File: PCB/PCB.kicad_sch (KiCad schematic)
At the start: 32 parts, among them J1 Conn_01x10_Socket, J10 DMX-OUT, J2 Conn_01x06, J3 Screw_Terminal_01x02, J4 TEST_1P, J5 DMX-IN, J6 TEST_1P, Q1 BC847W, Q2 BC847W, Q3 BC847W, SW2 SW_Coded_SH-7010, U1 SP3485CN, U3 ESP32-WROOM

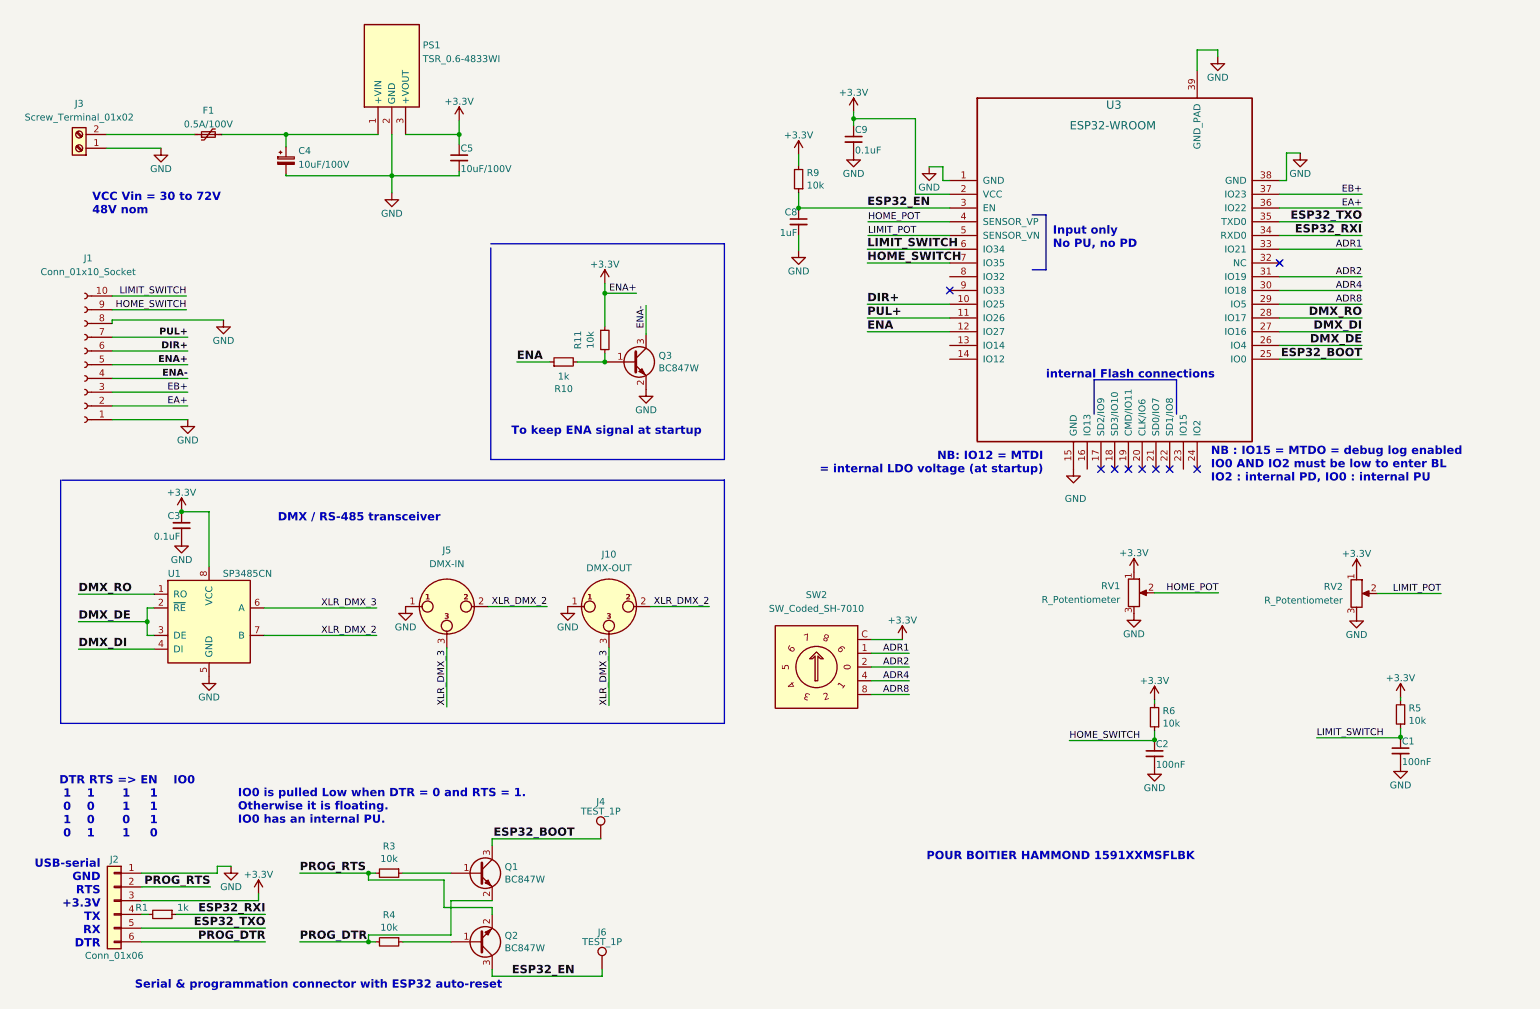
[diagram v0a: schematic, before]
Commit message: add expansion port and level shifter in progress
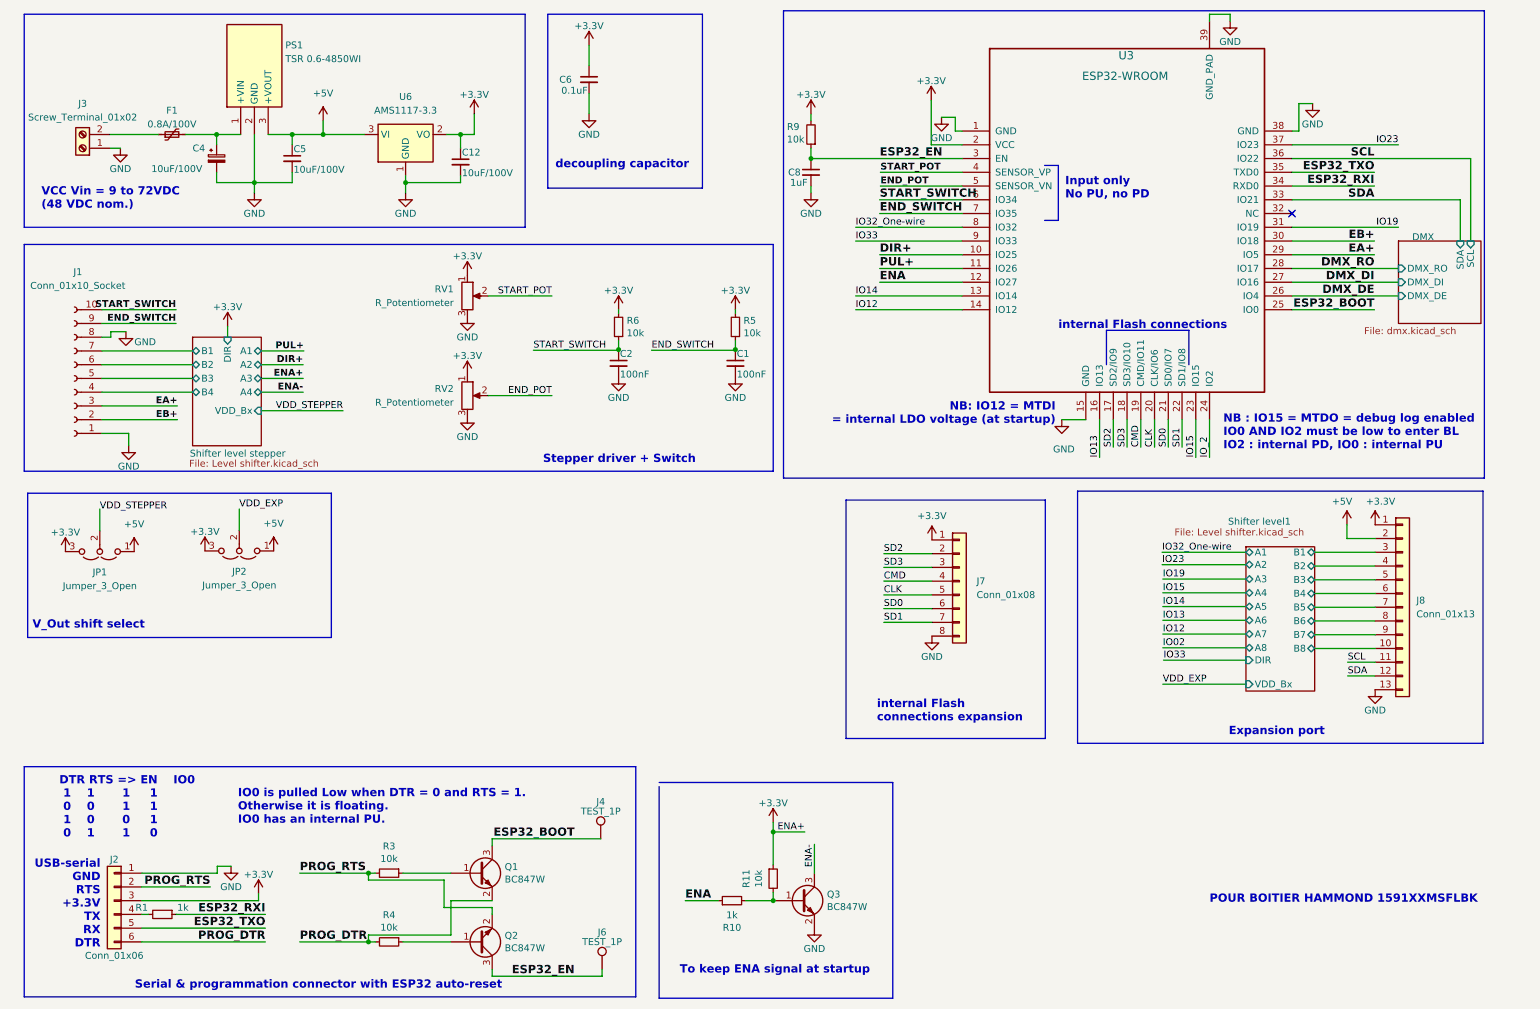
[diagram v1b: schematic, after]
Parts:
- removed C3, C9: 0.1uF, Capacitor_SMD:C_0603_1608Metric, symbol Device:C_Small
- removed J10: DMX-OUT, AC3MAH-AU-PRE:AC3MAH-AU-PRE, symbol Connector:XLR3
- removed J5: DMX-IN, AC3MAH-AU-PRE:AC3FAHL2-AU-PRE, symbol Connector:XLR3
- removed SW2: SW_Coded_SH-7010, Button_Switch_THT:Nidec_SD-2011, symbol Switch:SW_Coded_SH-7010
- removed U1: SP3485CN, Package_SO:SOIC-8_3.9x4.9mm_P1.27mm, symbol Interface_UART:SP3485CN
- added C12: 10uF/100V, Capacitor_SMD:C_1210_3225Metric, symbol Device:C_Small
- added C6: 0.1uF, Capacitor_SMD:C_0603_1608Metric, symbol Device:C_Small
- added J7: Conn_01x08, Connector_PinHeader_2.54mm:PinHeader_1x08_P2.54mm_Horizontal, symbol Connector_Generic:Conn_01x08
- added J8: Conn_01x13, Connector_PinHeader_2.54mm:PinHeader_1x13_P2.54mm_Horizontal, symbol Connector_Generic:Conn_01x13
- added JP1, JP2: Jumper_3_Open, Connector_PinHeader_2.54mm:PinHeader_1x03_P2.54mm_Vertical, symbol Jumper:Jumper_3_Open
- added U6: AMS1117-3.3, Package_TO_SOT_SMD:SOT-223-3_TabPin2, symbol Regulator_Linear:AMS1117-3.3
- F1: value 0.5A/100V -> 0.8A/100V
- PS1: value TSR_0.6-4833WI -> TSR 0.6-4850WI
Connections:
- net ADR4 is gone; now on net EB+: U3.30 (IO18)
- net ADR8 is gone; now on net EA+: U3.29 (IO5)
- net +3V3: now also C12.1, C6.1, J7.1 (Pin_1), J8.1 (Pin_1), JP1.3 (B), JP2.3 (B), U6.2 (VO); no longer C5.1, J1.5 (Pin_5), PS1.3 (+VOUT)
- net DIR+: no longer J1.6 (Pin_6)
- net EA+: now also J1.3 (Pin_3); no longer J1.2 (Pin_2), U3.36 (IO22)
- net EB+: now also J1.2 (Pin_2); no longer J1.3 (Pin_3), U3.37 (IO23)
- net ENA-: no longer J1.4 (Pin_4)
- net GND: now also C12.2, C6.2, J7.8 (Pin_8), J8.13 (Pin_13), U6.1 (GND)
- net PUL+: no longer J1.7 (Pin_7)
- net IO14: now reaches U3.13 (IO14)
- net IO12: now reaches U3.14 (IO12)
- net IO13: now reaches U3.16 (IO13)
- net SD2: now reaches U3.17 (SD2/IO9)
- net SD2: now also J7.2 (Pin_2)
- net SD3: now reaches U3.18 (SD3/IO10)
- net SD3: now also J7.3 (Pin_3)
- net CMD: now reaches U3.19 (CMD/IO11)
- net CMD: now also J7.4 (Pin_4)
- net CLK: now reaches U3.20 (CLK/IO6)
- net CLK: now also J7.5 (Pin_5)
- net SD0: now reaches U3.21 (SD0/IO7)
- net SD0: now also J7.6 (Pin_6)
- net SD1: now reaches U3.22 (SD1/IO8)
- net SD1: now also J7.7 (Pin_7)
- net IO15: now reaches U3.23 (IO15)
- net IO_2: now reaches U3.24 (IO2)
- net IO32_One-wire: now reaches U3.8 (IO32)
- net IO33: now reaches U3.9 (IO33)
- net ADR1 renamed SDA
- net SDA: now also J8.12 (Pin_12)
- net ADR2 renamed IO19
- net HOME_POT renamed START_POT
- net HOME_SWITCH renamed END_SWITCH
- net END_SWITCH: now also C1.1, R5.1; no longer C2.1, R6.1
- net LIMIT_POT renamed END_POT
- net LIMIT_SWITCH renamed START_SWITCH
- net START_SWITCH: now also C2.1, R6.1; no longer C1.1, R5.1
- new net +5V: C5.1, J8.2 (Pin_2), JP1.1 (A), JP2.1 (A), PS1.3 (+VOUT), U6.3 (VI)
- new net IO23: U3.37 (IO23)
- new net SCL: J8.11 (Pin_11), U3.36 (IO22)
- new net Shifter level stepper/B1: J1.7 (Pin_7)
- new net Shifter level stepper/B2: J1.6 (Pin_6)
- new net Shifter level stepper/B3: J1.5 (Pin_5)
- new net Shifter level stepper/B4: J1.4 (Pin_4)
- new net Shifter level1/B1: J8.3 (Pin_3)
- new net Shifter level1/B2: J8.4 (Pin_4)
- new net Shifter level1/B3: J8.5 (Pin_5)
- new net Shifter level1/B4: J8.6 (Pin_6)
- new net Shifter level1/B5: J8.7 (Pin_7)
- new net Shifter level1/B6: J8.8 (Pin_8)
- new net Shifter level1/B7: J8.9 (Pin_9)
- new net Shifter level1/B8: J8.10 (Pin_10)
- new net VDD_EXP: JP2.2 (C)
- new net VDD_STEPPER: JP1.2 (C)
- no-connect marks 9 -> 1
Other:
- added sheet DMX (dmx.kicad_sch)
- added sheet Shifter level stepper (Level shifter.kicad_sch)
- added sheet Shifter level1 (Level shifter.kicad_sch)
- note added: "Expansion port"
- note added: "Stepper driver + Switch"
- note added: "VCC Vin = 9 to 72VDC (48 VDC nom.)"
- note added: "V_Out shift select"
- note added: "decoupling capacitor"
- note added: "internal Flash connections expansion"
- note removed: "DMX / RS-485 transceiver"
- note removed: "VCC Vin = 30 to 72V 48V nom"
- company: (none) -> l'électron rare
- title: (none) -> DMX_ESP_Stepper-controler
- moved on the sheet: C1, C2, C4, C5, C8, F1, J1, J3, PS1, Q3, R10, R11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
